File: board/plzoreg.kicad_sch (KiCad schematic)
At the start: 62 parts, among them J1 IN, J2 Heatsink PE, J3 OUT, J4 AUX, Q1 BTA24-600C, U1 HLK-PM03, U3 LTV-817S, U4 MOC3023M, U5 PY32F030K2xTx, U6 LTV-354T, X1 SWD

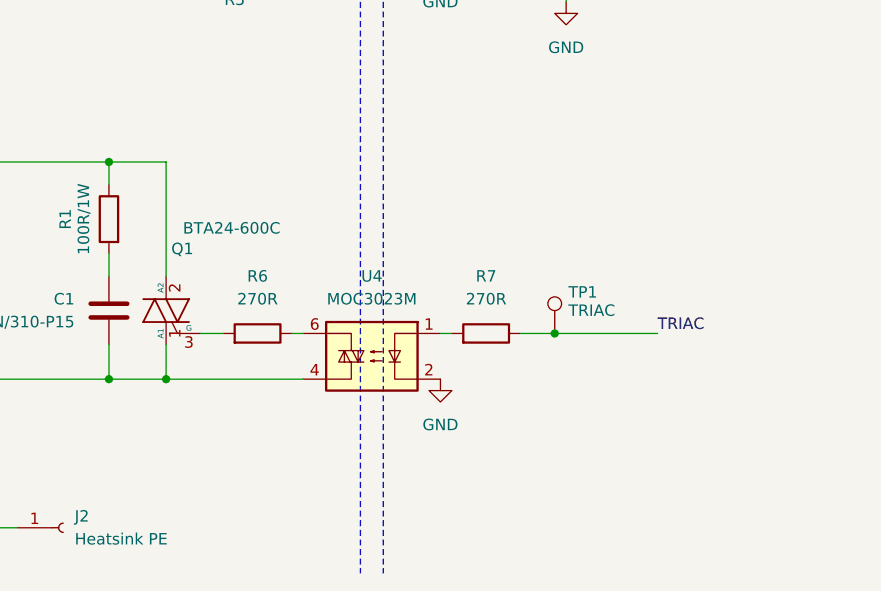
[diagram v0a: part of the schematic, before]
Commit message: v1.1: fixed triac gate issue
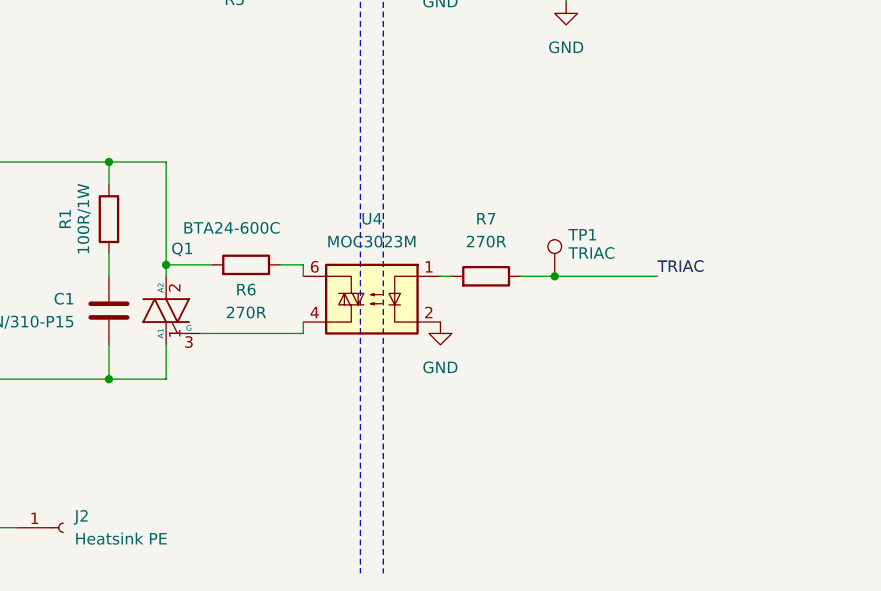
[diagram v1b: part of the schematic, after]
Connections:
- net MAINS_L_IN: now also R6.2
- net MAINS_L_OUT: no longer U4.4
- net at Q1.3 (G): now also U4.4; no longer R6.2
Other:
- moved on the sheet: R6, R7, TP1, U4
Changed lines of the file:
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@@
 	)
 	(junction
-		(at 105.41 166.37)
+		(at 105.41 160.02)
 		(diameter 0)
 		(color 0 0 0 0)
@@
 	)
 	(junction
+		(at 62.23 158.75)
+		(diameter 0)
+		(color 0 0 0 0)
+	)
+	(junction
 		(at 163.83 55.88)
 		(diameter 0)
@@
 	)
 	(junction
-		(at 62.23 171.45)
-		(diameter 0)
-		(color 0 0 0 0)
-	)
-	(junction
 		(at 111.76 39.37)
 		(diameter 0)
@@
 	(wire
 		(pts
-			(xy 116.84 166.37) (xy 105.41 166.37)
+			(xy 74.93 158.75) (xy 77.47 158.75)
+		)
+		(stroke
+			(width 0)
+			(type default)
+		)
+	)
+	(wire
+		(pts
+			(xy 116.84 160.02) (xy 105.41 160.02)
 		)
 		(stroke
@@
 	(wire
 		(pts
+			(xy 77.47 158.75) (xy 77.47 160.02)
+		)
+		(stroke
+			(width 0)
+			(type default)
+		)
+	)
+	(wire
+		(pts
 			(xy 177.8 109.22) (xy 179.07 109.22)
 		)
@@
 	(wire
 		(pts
-			(xy 105.41 166.37) (xy 101.6 166.37)
+			(xy 105.41 160.02) (xy 101.6 160.02)
 		)
 		(stroke
@@
 	(wire
 		(pts
-			(xy 62.23 147.32) (xy 62.23 160.02)
-		)
-		(stroke
-			(width 0)
-			(type default)
-		)
-	)
-	(wire
-		(pts
-			(xy 68.58 166.37) (xy 66.04 166.37)
+			(xy 66.04 166.37) (xy 77.47 166.37)
 		)
 		(stroke
@@
 		)
 	)
+	(wire
+		(pts
+			(xy 62.23 158.75) (xy 62.23 160.02)
+		)
+		(stroke
+			(width 0)
+			(type default)
+		)
+	)
 	(polyline
 		(pts
@@
 	(wire
 		(pts
-			(xy 77.47 171.45) (xy 62.23 171.45)
+			(xy 77.47 165.1) (xy 77.47 166.37)
 		)
 		(stroke
@@
 	(wire
 		(pts
-			(xy 93.98 166.37) (xy 92.71 166.37)
+			(xy 93.98 160.02) (xy 92.71 160.02)
 		)
 		(stroke
@@
 	(wire
 		(pts
-			(xy 212.09 146.05) (xy 212.09 148.59)
+			(xy 62.23 147.32) (xy 62.23 158.75)
 		)
 		(stroke
@@
 	(wire
 		(pts
-			(xy 231.14 86.36) (xy 231.14 93.98)
+			(xy 62.23 158.75) (xy 67.31 158.75)
+		)
+		(stroke
+			(width 0)
+			(type default)
+		)
+	)
+	(wire
+		(pts
+			(xy 212.09 146.05) (xy 212.09 148.59)
 		)
 		(stroke
@@
 	(wire
 		(pts
-			(xy 76.2 166.37) (xy 77.47 166.37)
+			(xy 231.14 86.36) (xy 231.14 93.98)
 		)
 		(stroke
@@
 	)
 	(label "TRIAC"
-		(at 116.84 166.37 0)
+		(at 116.84 160.02 0)
 		(effects
 			(font
@@
 	(symbol
 		(lib_id "power:GND")
-		(at 92.71 171.45 0)
+		(at 92.71 165.1 0)
 		(mirror y)
 		(unit 1)
@@
 		(fields_autoplaced yes)
 		(property "Reference" "#PWR03"
-			(at 92.71 177.8 0)
+			(at 92.71 171.45 0)
 			(effects
 				(font
@@
 		)
 		(property "Value" "GND"
-			(at 92.71 176.53 0)
+			(at 92.71 170.18 0)
 			(effects
 				(font
@@
 		)
 		(property "Footprint" ""
-			(at 92.71 171.45 0)
+			(at 92.71 165.1 0)
 			(effects
 				(font
@@
 		)
 		(property "Datasheet" ""
-			(at 92.71 171.45 0)
+			(at 92.71 165.1 0)
 			(effects
 				(font
@@
 		)
 		(property "Description" "Power symbol creates a global label with name \"GND\" , ground"
-			(at 92.71 171.45 0)
+			(at 92.71 165.1 0)
 			(effects
 				(font
@@
 	(symbol
 		(lib_id "Device:R")
-		(at 97.79 166.37 270)
+		(at 97.79 160.02 270)
 		(mirror x)
 		(unit 1)
@@
 		(fields_autoplaced yes)
 		(property "Reference" "R7"
-			(at 97.79 160.02 90)
+			(at 97.79 153.67 90)
 			(effects
 				(font
@@
 		)
 		(property "Value" "270R"
-			(at 97.79 162.56 90)
+			(at 97.79 156.21 90)
 			(effects
 				(font
@@
 		)
 		(property "Footprint" "Resistor_SMD:R_0805_2012Metric_Pad1.20x1.40mm_HandSolder"
-			(at 97.79 168.148 90)
+			(at 97.79 161.798 90)
 			(effects
 				(font
@@
 		)
 		(property "Datasheet" "~"
-			(at 97.79 166.37 0)
+			(at 97.79 160.02 0)
 			(effects
 				(font
@@
 		)
 		(property "Description" "Resistor"
-			(at 97.79 166.37 0)
+			(at 97.79 160.02 0)
 			(effects
 				(font
@@
 	(symbol
 		(lib_id "Relay_SolidState:MOC3023M")
-		(at 85.09 168.91 0)
+		(at 85.09 162.56 0)
 		(mirror y)
 		(unit 1)
@@
 		(fields_autoplaced yes)
 		(property "Reference" "U4"
-			(at 85.09 160.02 0)
+			(at 85.09 153.67 0)
 			(effects
 				(font
@@
 		)
 		(property "Value" "MOC3023M"
-			(at 85.09 162.56 0)
+			(at 85.09 156.21 0)
 			(effects
 				(font
@@
 		)
 		(property "Footprint" "Package_DIP:DIP-6_W8.89mm_SMDSocket_LongPads"
-			(at 90.17 173.99 0)
+			(at 90.17 167.64 0)
 			(effects
 				(font
@@
 		)
 		(property "Datasheet" "https://www.onsemi.com/pub/Collateral/MOC3023M-D.PDF"
-			(at 85.09 168.91 0)
+			(at 85.09 162.56 0)
 			(effects
 				(font
@@
 		)
 		(property "Description" "Random Phase Opto-Triac, Vdrm 400V, Ift 5mA, DIP6"
-			(at 85.09 168.91 0)
+			(at 85.09 162.56 0)
 			(effects
 				(font
@@
 	(symbol
 		(lib_id "Device:R")
-		(at 72.39 166.37 270)
+		(at 71.12 158.75 270)
 		(mirror x)
 		(unit 1)
@@
 		(on_board yes)
 		(dnp no)
-		(fields_autoplaced yes)
 		(property "Reference" "R6"
-			(at 72.39 160.02 90)
+			(at 71.12 161.544 90)
 			(effects
 				(font
@@
 		)
 		(property "Value" "270R"
-			(at 72.39 162.56 90)
+			(at 71.12 164.084 90)
 			(effects
 				(font
@@
 		)
 		(property "Footprint" "Resistor_THT:R_Axial_DIN0207_L6.3mm_D2.5mm_P10.16mm_Horizontal"
-			(at 72.39 168.148 90)
+			(at 71.12 160.528 90)
 			(effects
 				(font
@@
 		)
 		(property "Datasheet" "~"
-			(at 72.39 166.37 0)
+			(at 71.12 158.75 0)
 			(effects
 				(font
@@
 		)
 		(property "Description" "Resistor"
-			(at 72.39 166.37 0)
+			(at 71.12 158.75 0)
 			(effects
 				(font
@@
 	(symbol
 		(lib_id "Connector:TestPoint")
-		(at 105.41 166.37 0)
+		(at 105.41 160.02 0)
 		(unit 1)
 		(exclude_from_sim no)
@@
 		(dnp no)
 		(property "Reference" "TP1"
-			(at 106.934 161.798 0)
+			(at 106.934 155.448 0)
 			(effects
 				(font
@@
 		)
 		(property "Value" "TRIAC"
-			(at 106.934 163.83 0)
+			(at 106.934 157.48 0)
 			(effects
 				(font
@@
 		)
 		(property "Footprint" "TestPoint:TestPoint_THTPad_D2.0mm_Drill1.0mm"
-			(at 110.49 166.37 0)
+			(at 110.49 160.02 0)
 			(effects
 				(font
@@
 		)
 		(property "Datasheet" "~"
-			(at 110.49 166.37 0)
+			(at 110.49 160.02 0)
 			(effects
 				(font
@@
 		)
 		(property "Description" "test point"
-			(at 105.41 166.37 0)
+			(at 105.41 160.02 0)
 			(effects
 				(font
